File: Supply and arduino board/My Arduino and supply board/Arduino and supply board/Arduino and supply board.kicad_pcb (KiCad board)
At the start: 2 copper layers, 44.5 x 57.2 mm, 62 parts, among them J1 USB_C_Receptacle_USB2.0, J2 Conn_01x03, J3 Conn_01x03, J4 Conn_01x03, J5 Conn_01x03, J6 Conn_01x03, J7 Conn_01x03, Q2 16MHz, T1 FDN340V, U1 LM358D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

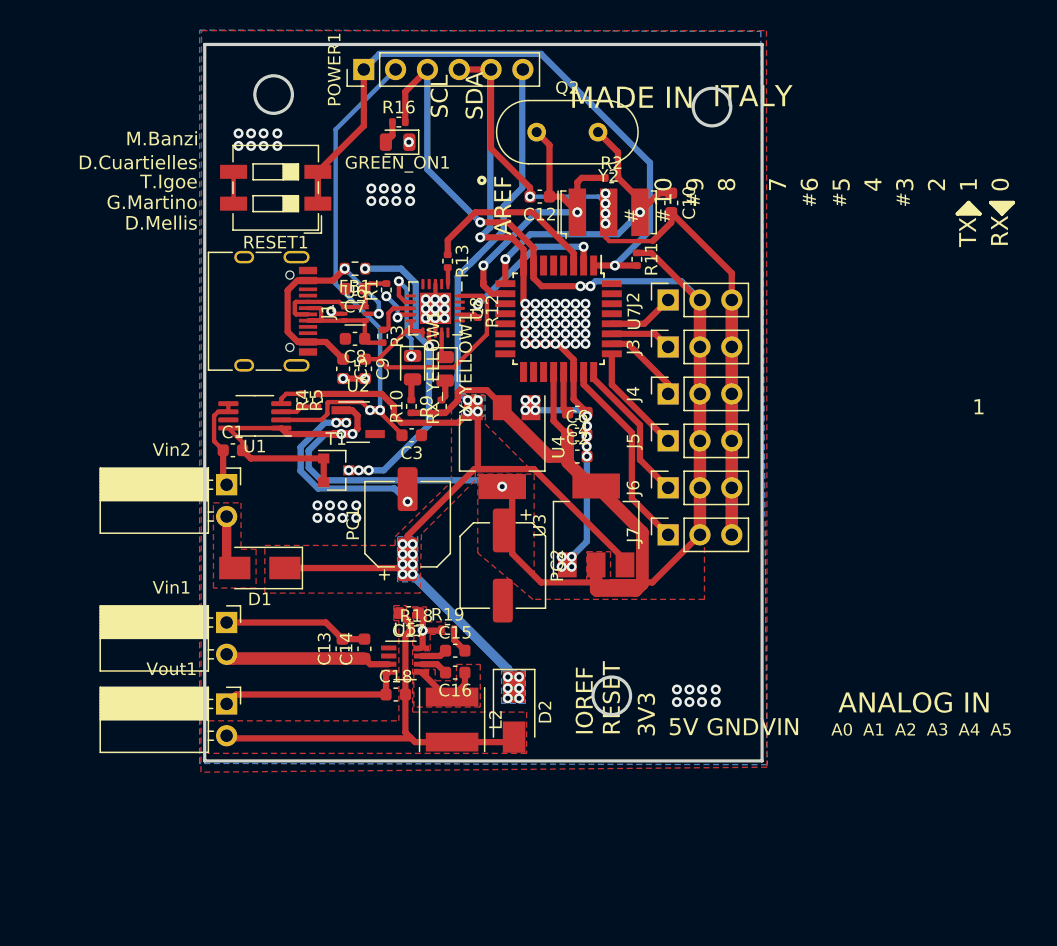
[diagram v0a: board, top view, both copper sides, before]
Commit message: change power supply 24v to 12v and 12v to 5v
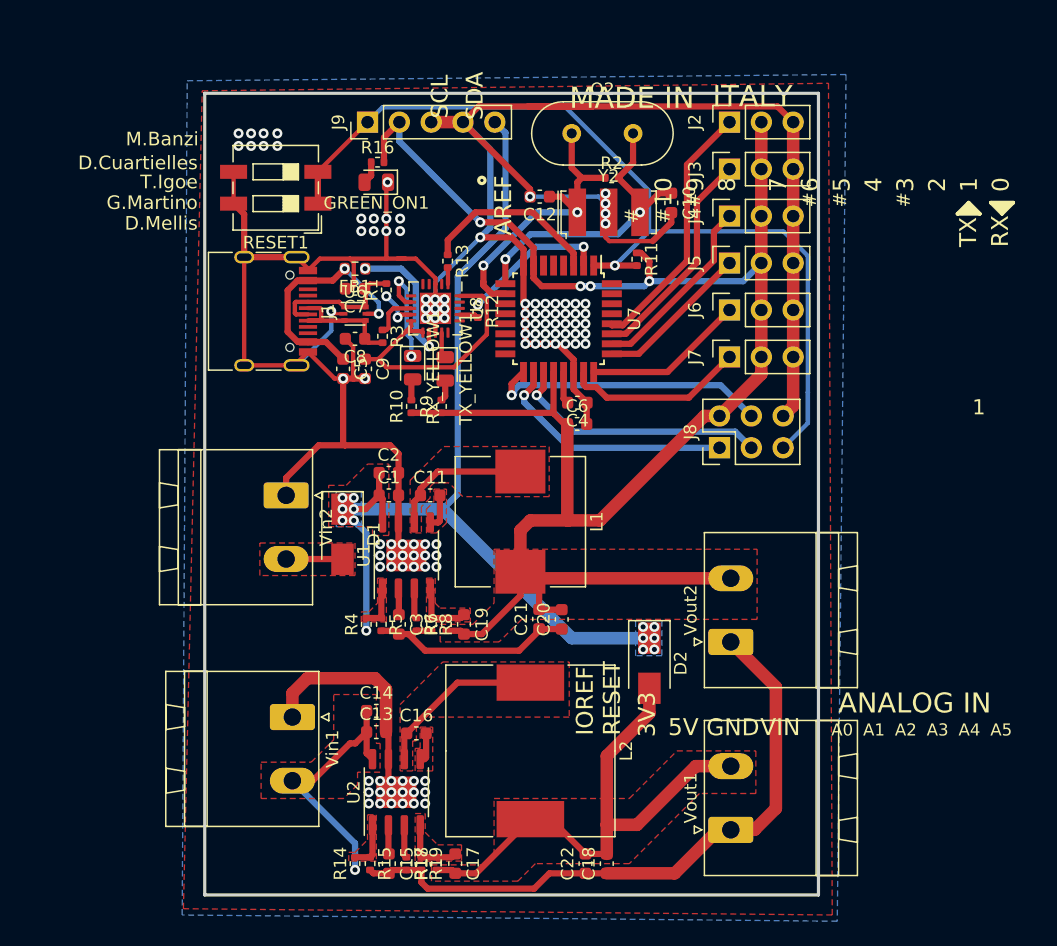
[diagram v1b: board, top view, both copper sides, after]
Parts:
- removed PC1, PC2: 47u, Capacitor_SMD:CP_Elec_6.3x9.9
- removed POWER1: Conn_01x06, Connector_PinHeader_2.54mm:PinHeader_1x06_P2.54mm_Vertical
- removed T1: FDN340V, Package_TO_SOT_SMD:SOT-23
- removed U3: MC33269D-5.0, Package_TO_SOT_SMD:SOT-223-3_TabPin2
- removed U4: MC33269ST-5.0T3, Package_TO_SOT_SMD:SOT-223
- removed U5: TPS629DRL, Package_TO_SOT_SMD:TSOT-23-8
- added C11: 0.1u, Capacitor_SMD:C_0603_1608Metric, F.Cu at (150.2, 76.1)
- added C19: 680p, Capacitor_SMD:C_0603_1608Metric, F.Cu at (152.9, 86.4)
- added C20: 47u, Capacitor_SMD:C_0603_1608Metric, F.Cu at (160.7, 86.0)
- added C21: 47u, Capacitor_SMD:C_0603_1608Metric, F.Cu at (158.9, 85.9)
- added C22: 47u, Capacitor_SMD:C_0603_1608Metric, F.Cu at (162.6, 105.5)
- added J8: Programing_port, Connector_PinHeader_2.54mm:PinHeader_2x03_P2.54mm_Vertical, F.Cu at (173.3, 72.3)
- added J9: Conn_01x05, Connector_PinHeader_2.54mm:PinHeader_1x05_P2.54mm_Vertical, F.Cu at (145.2, 46.3)
- added L1: 33u, Inductor_SMD:L_Wuerth_HCI-1040, F.Cu at (157.4, 78.2)
- added R14: 100K, Resistor_SMD:R_0402_1005Metric, F.Cu at (144.2, 105.5)
- added R15: 5.6K, Resistor_SMD:R_0402_1005Metric, F.Cu at (145.4, 105.5)
- added R17: 33K, Resistor_SMD:R_0402_1005Metric, F.Cu at (148.3, 105.5)
- added R6: 82K, Resistor_SMD:R_0402_1005Metric, F.Cu at (149.1, 86.4)
- added R7: 11K, Resistor_SMD:R_0402_1005Metric, F.Cu at (151.5, 86.4)
- added R8: 43K, Resistor_SMD:R_0402_1005Metric, F.Cu at (150.3, 86.4)
- added Vout2: +5V_out, Connector_Phoenix_MSTB:PhoenixContact_MSTBA_2,5_2-G-5,08_1x02_P5.08mm_Horizontal, F.Cu at (174.2, 87.8)
- C1: value 100n -> 10u
- C15: value 33n -> 1u
- C16: value 100n -> 0.1u
- C17: value 47p -> 680p
- L2: value 15u -> 47u; footprint Inductor_SMD:L_Taiyo-Yuden_MD-5050 -> Inductor_SMD:L_Wuerth_HCM-1350
- R18: value 140K -> 110K
- R4: value 10K -> 100K
- R5: value 10K -> 12K
- U1: value LM358D -> MP4581GN-P; footprint Package_SO:MSOP-8_3x3mm_P0.65mm -> Package_SO:SOIC-8-1EP_3.9x4.9mm_P1.27mm_EP2.514x3.2mm
- U2: value LP2985-3.3 -> MP4581GN-P; footprint Package_TO_SOT_SMD:SOT-23-5_HandSoldering -> Package_SO:SOIC-8-1EP_3.9x4.9mm_P1.27mm_EP2.514x3.2mm
- Vin1: value Conn_01x02 -> +24V_in; footprint Connector_PinSocket_2.54mm:PinSocket_1x02_P2.54mm_Horizontal -> Connector_Phoenix_MSTB:PhoenixContact_MSTBA_2,5_2-G-5,08_1x02_P5.08mm_Horizontal
- Vin2: value Conn_01x02 -> +12V_in; footprint Connector_PinSocket_2.54mm:PinSocket_1x02_P2.54mm_Horizontal -> Connector_Phoenix_MSTB:PhoenixContact_MSTBA_2,5_2-G-5,08_1x02_P5.08mm_Horizontal
- Vout1: value Conn_01x02 -> +12V_out; footprint Connector_PinSocket_2.54mm:PinSocket_1x02_P2.54mm_Horizontal -> Connector_Phoenix_MSTB:PhoenixContact_MSTBA_2,5_2-G-5,08_1x02_P5.08mm_Horizontal
- moved Vout1 41.5 mm to (174.2, 102.8), turned to 90 degrees
- moved U2 29.7 mm to (147.5, 99.8), turned to 90 degrees
- moved C18 21.6 mm to (164.3, 105.5), turned to 90 degrees
- moved C17 20.3 mm to (152.2, 105.5), turned to 270 degrees
- moved R5 19.0 mm to (146.3, 86.4)
- moved R19 18.8 mm to (149.5, 105.5), turned to 270 degrees
- moved R18 18.7 mm to (150.7, 105.5), turned to 90 degrees
- moved R4 18.3 mm to (145.1, 86.4)
- moved C15 17.8 mm to (146.9, 105.5), turned to 270 degrees
- moved U1 16.5 mm to (148.3, 80.9), turned to 90 degrees
- moved C3 15.1 mm to (147.7, 86.4), turned to 270 degrees
- moved C2 15.1 mm to (146.9, 74.3)
- moved J2 15.0 mm to (174.1, 46.3)
- moved J3 15.0 mm to (174.1, 50.0)
- moved J4 15.0 mm to (174.1, 53.8)
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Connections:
- net /PWRIM renamed Net-(D1-Pad2)
- net Net-(C17-Pad2) renamed /VOUT+12V
- C1 pad 1: GND -> /VIN+12V
- C1 pad 2: +5V -> GND
- C13 pad 1: Net-(C13-Pad1) -> /VIN+24V
- C14 pad 1: Net-(C13-Pad1) -> /VIN+24V
- C2 pad 1: +5V -> /VIN+12V
- C3 pad 1: GND -> Net-(C3-Pad1)
- C3 pad 2: /+3V3 -> GND
- D1 pad 1: /VIN -> /VIN+12V
- D2 pad 1: /VIN -> /VIN+12V
- R4 pad 1: /CMP -> /VIN+12V
- R4 pad 2: /VIN -> Net-(R4-Pad2)
- R5 pad 1: GND -> Net-(R4-Pad2)
- R5 pad 2: /CMP -> GND
- U1 pad 1: +5V -> Net-(R4-Pad2)
- U1 pad 2: /+3V3 -> Net-(C3-Pad1)
- U1 pad 3: /CMP -> Net-(R6-Pad1)
- U1 pad 4: GND -> Net-(C19-Pad1)
- U1 pad 5: GND -> Net-(C11-Pad2)
- U1 pad 6: GND -> Net-(C11-Pad1)
- U1 pad 7: (no net) -> GND
- U1 pad 8: +5V -> /VIN+12V
- U2 pad 1: +5V -> Net-(R14-Pad2)
- U2 pad 2: GND -> Net-(C15-Pad1)
- U2 pad 3: +5V -> Net-(R17-Pad1)
- U2 pad 4: (no net) -> Net-(C17-Pad1)
- U2 pad 5: /+3V3 -> Net-(C16-Pad2)
- U7 pad 17: (no net) -> /MOSI
- U7 pad 18: (no net) -> /MISO
- U7 pad 19: (no net) -> /SCK
- Vin1 pad 2: Net-(C13-Pad1) -> /VIN+24V
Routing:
- net GND: track 170.1 -> 300.9 mm, vias 102 -> 106
- net /VIN: track 98.9 -> 0.00 mm, vias 18 -> 0
- net /VIN+12V: track 0.00 -> 82.5 mm, vias 0 -> 13
- net /+3V3: track 42.6 -> 0.00 mm, vias 2 -> 0
- net +5V: track 189.2 -> 149.1 mm, vias 6 -> 4
- net /RESET: track 52.0 -> 76.3 mm
- net /MOSI: track 0.00 -> 22.9 mm, vias 0 -> 1
- net /SCK: track 0.00 -> 21.0 mm, vias 0 -> 1
- net /VIN+24V: track 0.00 -> 20.8 mm, vias 0 -> 1
- net /MISO: track 0.00 -> 19.8 mm, vias 0 -> 1
- net /USBVCC: track 30.7 -> 14.9 mm, vias 5 -> 2
- net /AD5: track 5.29 -> 20.7 mm
- net Net-(C13-Pad1): track 13.3 -> 0.00 mm
- net /AD4: track 4.93 -> 17.7 mm
- net Net-(C11-Pad1): track 0.00 -> 11.4 mm
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- added copper zone on B.Cu, net /VIN+12V
- added copper zone on F.Cu, net /VIN+12V
- added copper zone on F.Cu, net /VIN+24V
- added copper zone on F.Cu, net Net-(C11-Pad1)
- added copper zone on F.Cu, net Net-(C11-Pad2)
- added copper zone on F.Cu, net Net-(C16-Pad2)
- added copper zone on F.Cu, net Net-(C19-Pad1)
- added copper zone on F.Cu, net Net-(R14-Pad2)
- added copper zone on F.Cu, net Net-(R4-Pad2)
- removed copper zone on B.Cu, net /VIN
- removed copper zone on F.Cu, net /VIN
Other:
- board size 44.5 x 57.2 mm -> 49 x 64 mm
- board text removed: "12Vin"
- board text removed: "12Vout"
- board text removed: "24Vin"
- board text removed: "D:/SmartProjects/Snc/a4_bn_logo2.bmp"

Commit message: generate blueprints for lose part feeder
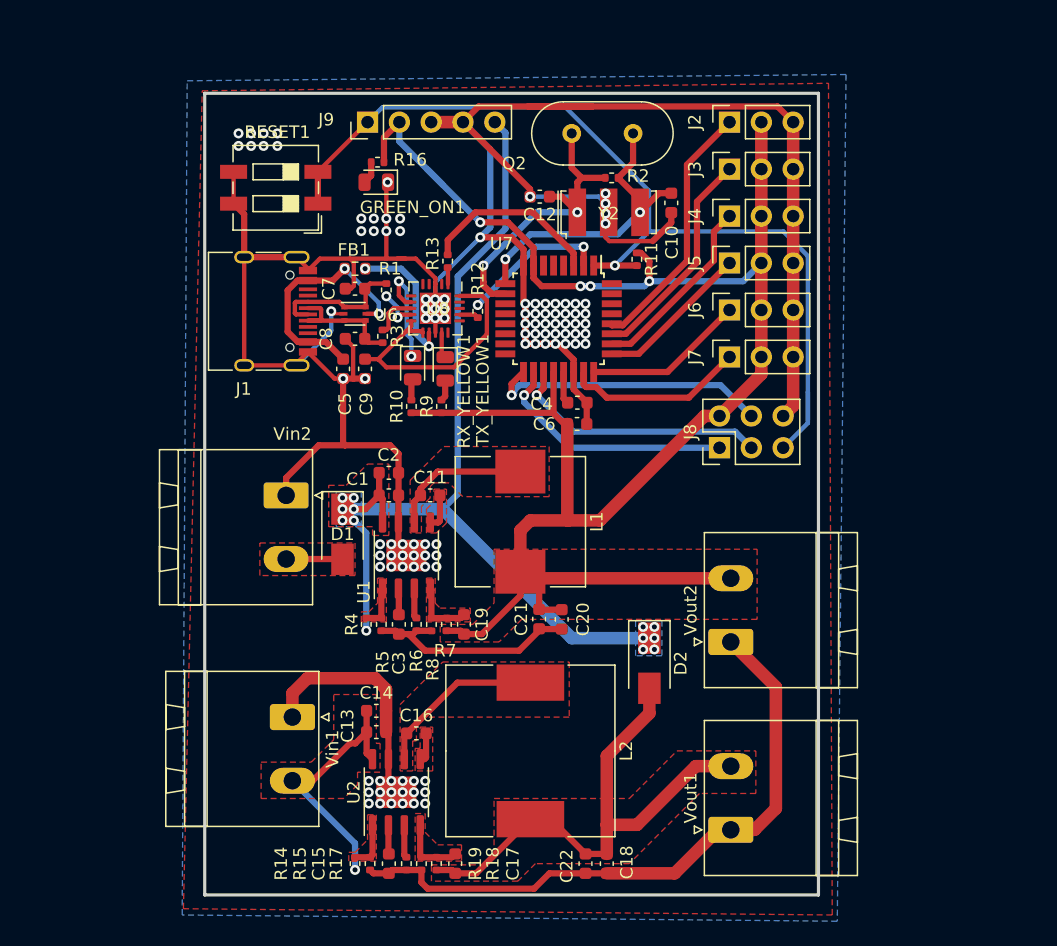
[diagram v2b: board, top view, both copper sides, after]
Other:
- board text removed: "#"
- board text removed: "0"
- board text removed: "1"
- board text removed: "10"
- board text removed: "2"
- board text removed: "3"
- board text removed: "3V3"
- board text removed: "4"
- board text removed: "5"
- board text removed: "5V"
- board text removed: "6"
- board text removed: "7"
- board text removed: "8"
- board text removed: "9"
- board text removed: "A0"
- board text removed: "A1"
- board text removed: "A2"
- board text removed: "A3"
- board text removed: "A4"
- board text removed: "A5"
- board text removed: "ANALOG IN"
- board text removed: "AREF"
- board text removed: "D.Cuartielles"
- board text removed: "D.Mellis"
- board text removed: "G.Martino"
- board text removed: "GND"
- board text removed: "IOREF"
- board text removed: "ITALY"
- board text removed: "M.Banzi"
- board text removed: "MADE IN"
- board text removed: "RESET"
- board text removed: "RX"
- board text removed: "SCL"
- board text removed: "SDA"
- board text removed: "T.Igoe"
- board text removed: "TX"
- board text removed: "VIN"

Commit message: changes on powersuply
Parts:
- removed R15: 5.6K, Resistor_SMD:R_0402_1005Metric
- removed R5: 12K, Resistor_SMD:R_0402_1005Metric
- C15, C3: value 1u -> 0.1u
- C16: value 0.1u -> 10n
- C17: value 680p -> 3.9u
- C19: value 680p -> 3.9n
- L1: value 33u -> 220uH/1.6A; footprint Inductor_SMD:L_Wuerth_HCI-1040 -> Inductor_SMD:L_Wuerth_HCI-1350
- L2: value 47u -> 220uH/1.6A; footprint Inductor_SMD:L_Wuerth_HCM-1350 -> Inductor_SMD:L_Wuerth_HCI-1350
- R17: value 33K -> 6.8K
- R19: value 10K -> 9K
- R6: value 82K -> 6.8K
- R8: value 43K -> 2.4K
- U1, U2: value MP4581GN-P -> TD2786MR; footprint Package_SO:SOIC-8-1EP_3.9x4.9mm_P1.27mm_EP2.514x3.2mm -> Package_SO:SOP-8_3.9x4.9mm_P1.27mm
- moved C19 20.6 mm to (147.0, 106.1), turned to 180 degrees
- moved C17 17.2 mm to (149.8, 88.5), turned to 180 degrees
- moved C21 12.3 mm to (170.9, 83.3)
- moved C20 8.92 mm to (169.2, 83.3)
- moved C18 8.91 mm to (170.4, 99.0)
- moved C22 8.85 mm to (168.6, 99.0)
- moved R4 6.80 mm to (151.9, 86.4)
- moved C3 5.72 mm to (153.4, 86.9)
- moved R18 5.55 mm to (145.3, 104.2)
- moved C14 5.44 mm to (143.0, 97.9), turned to 90 degrees
- moved R14 5.07 mm to (149.1, 104.2)
- moved L1 4.25 mm to (161.2, 80.1)
- moved D2 3.98 mm to (169.6, 93.0)
- moved C2 3.83 mm to (145.6, 77.9), turned to 90 degrees
- moved C15 3.79 mm to (150.6, 104.7)
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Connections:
- C17 pad 2: /VOUT+12V -> GND
- C19 pad 2: +5V -> GND
- R17 pad 2: GND -> Net-(C19-Pad1)
- R18 pad 2: Net-(C17-Pad1) -> Net-(R18-Pad2)
- R19 pad 1: Net-(C17-Pad1) -> Net-(R18-Pad2)
- R6 pad 2: GND -> Net-(C17-Pad1)
- R7 pad 2: Net-(C19-Pad1) -> Net-(R7-Pad2)
- R8 pad 1: Net-(C19-Pad1) -> Net-(R7-Pad2)
- U1 pad 1: Net-(R4-Pad2) -> Net-(C11-Pad2)
- U1 pad 2: Net-(C3-Pad1) -> /VIN+12V
- U1 pad 3: Net-(R6-Pad1) -> Net-(C11-Pad1)
- U1 pad 4: Net-(C19-Pad1) -> GND
- U1 pad 5: Net-(C11-Pad2) -> Net-(R7-Pad2)
- U1 pad 6: Net-(C11-Pad1) -> Net-(R6-Pad1)
- U1 pad 7: GND -> Net-(R4-Pad2)
- U1 pad 8: /VIN+12V -> Net-(C3-Pad1)
- U2 pad 1: Net-(R14-Pad2) -> Net-(C16-Pad2)
- U2 pad 2: Net-(C15-Pad1) -> /VIN+24V
- U2 pad 3: Net-(R17-Pad1) -> Net-(C16-Pad1)
- U2 pad 4: Net-(C17-Pad1) -> GND
- U2 pad 5: Net-(C16-Pad2) -> Net-(R18-Pad2)
- U2 pad 6: Net-(C16-Pad1) -> Net-(R17-Pad1)
- U2 pad 7: GND -> Net-(R14-Pad2)
- U2 pad 8: /VIN+24V -> Net-(C15-Pad1)
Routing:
- net GND: track 300.9 -> 355.8 mm, vias 106 -> 70
- net /VOUT+12V: track 43.1 -> 36.2 mm, vias 0 -> 2
- net Net-(C17-Pad1): track 5.40 -> 1.60 mm
- net Net-(C19-Pad1): track 5.12 -> 1.40 mm
- net Net-(R7-Pad2): track 0.00 -> 3.57 mm
- net Net-(R18-Pad2): track 0.00 -> 3.37 mm
- net Net-(C11-Pad1): track 11.4 -> 13.6 mm
- net Net-(R14-Pad2): track 3.83 -> 2.08 mm
- net Net-(C16-Pad1): track 13.7 -> 15.4 mm
- net Net-(R4-Pad2): track 3.59 -> 2.29 mm
- net Net-(D1-Pad2): track 4.51 -> 5.31 mm
- net /VIN+12V: track 82.5 -> 83.2 mm, vias 13 -> 14
- net Net-(C11-Pad2): track 2.85 -> 2.27 mm
- net +5V: track 149.1 -> 148.5 mm, vias 4 -> 6
- net Net-(R17-Pad1): track 2.62 -> 2.09 mm
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- added copper zone on F.Cu, net Net-(C15-Pad1)
- added copper zone on F.Cu, net Net-(C3-Pad1)
- removed copper zone on F.Cu, net Net-(C16-Pad2)
- removed copper zone on F.Cu, net Net-(C17-Pad1)
- removed copper zone on F.Cu, net Net-(C19-Pad1)
- removed copper zone on F.Cu, net Net-(R14-Pad2)
- removed copper zone on F.Cu, net Net-(R4-Pad2)
